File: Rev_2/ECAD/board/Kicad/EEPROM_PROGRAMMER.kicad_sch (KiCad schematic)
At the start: 27 parts, among them Q1 PMOS, Q2 PNP, Q3 PNP, U1 FT232RL, U2 ATMega328P-AU, U3 ICSP, U4 SD_CARD_READER, Y1 16MHz

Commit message: Adde Summer, Read-LED, Write-LED
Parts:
- added D5: READ, LED_SMD:LED_0805_2012Metric_Pad1.15x1.40mm_HandSolder, symbol Device:LED
- added D6: WRITE, LED_SMD:LED_0805_2012Metric_Pad1.15x1.40mm_HandSolder, symbol Device:LED
- added Q4: NPN, Package_TO_SOT_SMD:SOT-23, symbol Simulation_SPICE:NPN
- added R10, R9: 4k7, Resistor_SMD:R_0805_2012Metric_Pad1.20x1.40mm_HandSolder, symbol Device:R
- added R11, R8: 10k, Resistor_SMD:R_0805_2012Metric_Pad1.20x1.40mm_HandSolder, symbol Device:R
- added U5: SUM, EEPROM_PROGRAMMER:Summer, symbol EEPROM_PROGRAMMER:Summer
- R1, R2, R3, R5, R6: value 5k1 -> 4k7
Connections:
- net D11/MOSI: now also R10.2
- net D12/MISO: now also R9.2
- net D13/SCK: now also R8.2
- net GND: now also Q4.3 (E)
- net SELECT: now reaches U2.14 ((SS)PB2), U4.4 (#CS)
- net SELECT: now also R11.2
- new net: D5.2 (A), R9.1
- new net: Q4.2 (B), R11.1
- new net: R8.1, U5.1 (+)
- new net: D6.2 (A), R10.1
- new net SELECT_GND: D5.1 (K), D6.1 (K), Q4.1 (C), U5.2 (-)

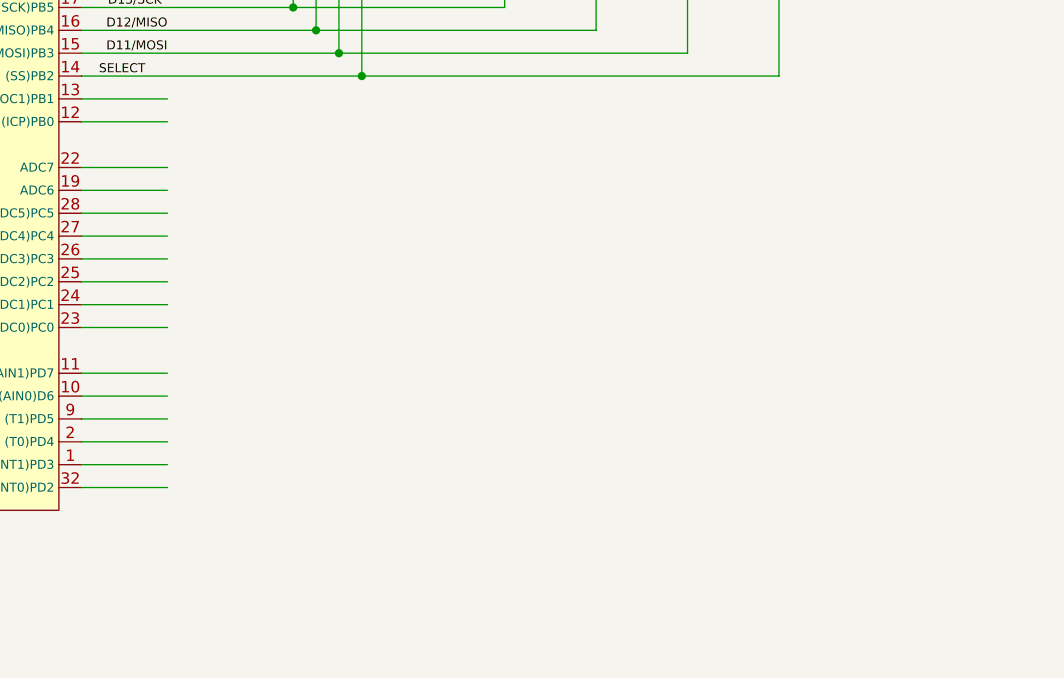
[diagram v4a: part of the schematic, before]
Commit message: Added registers for the EEPROM
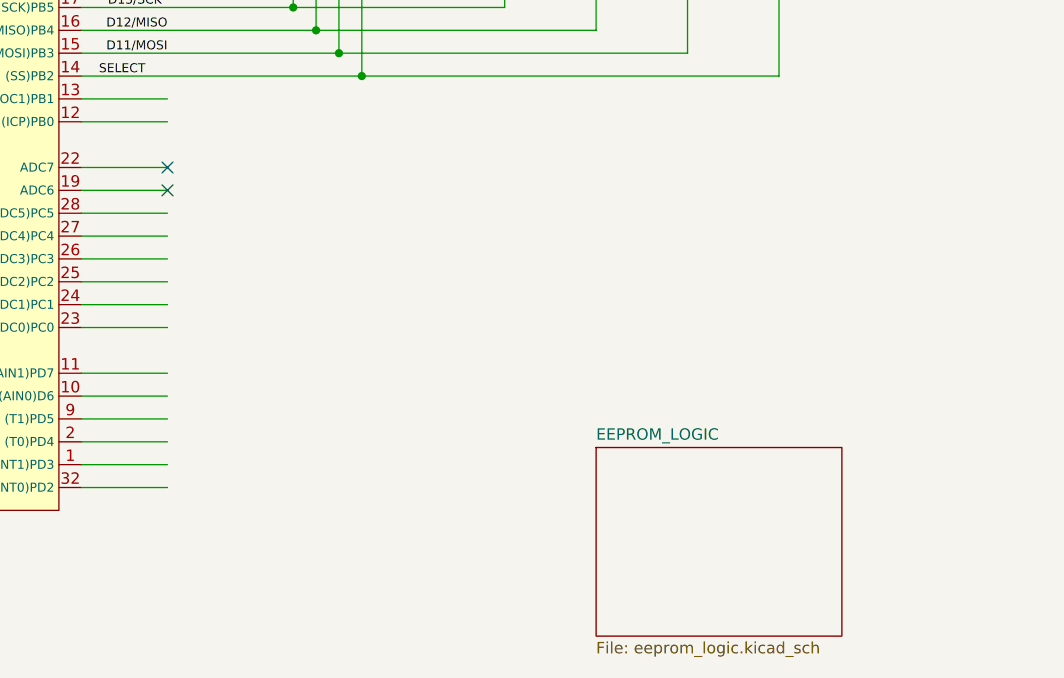
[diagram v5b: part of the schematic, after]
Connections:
- no-connect marks 1 -> 3
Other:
- added sheet EEPROM_LOGIC (eeprom_logic.kicad_sch)
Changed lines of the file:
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@@
   )
   (no_connect (at 31.75 48.895))
+  (no_connect (at 95.25 161.29))
+  (no_connect (at 95.25 158.75))
   (wire (pts (xy 78.74 46.355) (xy 78.74 50.8))
     (stroke (width 0) (type default))
@@
       )
     )
+  )
+  (sheet (at 142.875 189.865) (size 27.305 20.955) (fields_autoplaced)
+    (stroke (width 0.1524) (type solid))
+    (fill (color 0 0 0 0.0000))
+    (property "Sheetname" "EEPROM_LOGIC" (at 142.875 189.1534 0)
+      (effects (font (size 1.27 1.27)) (justify left bottom))
+    )
+    (property "Sheetfile" "eeprom_logic.kicad_sch" (at 142.875 211.4046 0)
+      (effects (font (size 1.27 1.27)) (justify left top))
+    )
+    (instances
+      (project "EEPROM_PROGRAMMER"
+        (path "/bc7d165f-daf1-4bac-b7f4-5fbe134c87cf" (page "2"))
+      )
+    )

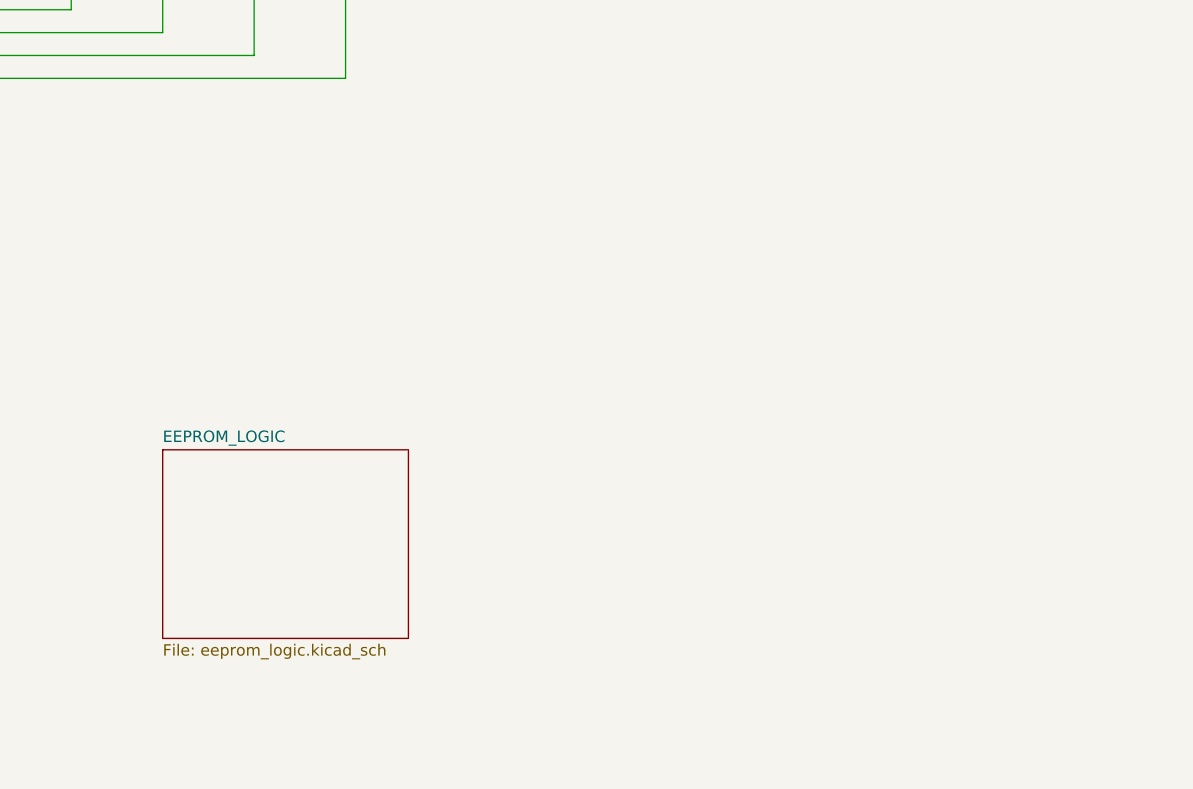
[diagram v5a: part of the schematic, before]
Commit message: Finished most of EEPROM LOGIC
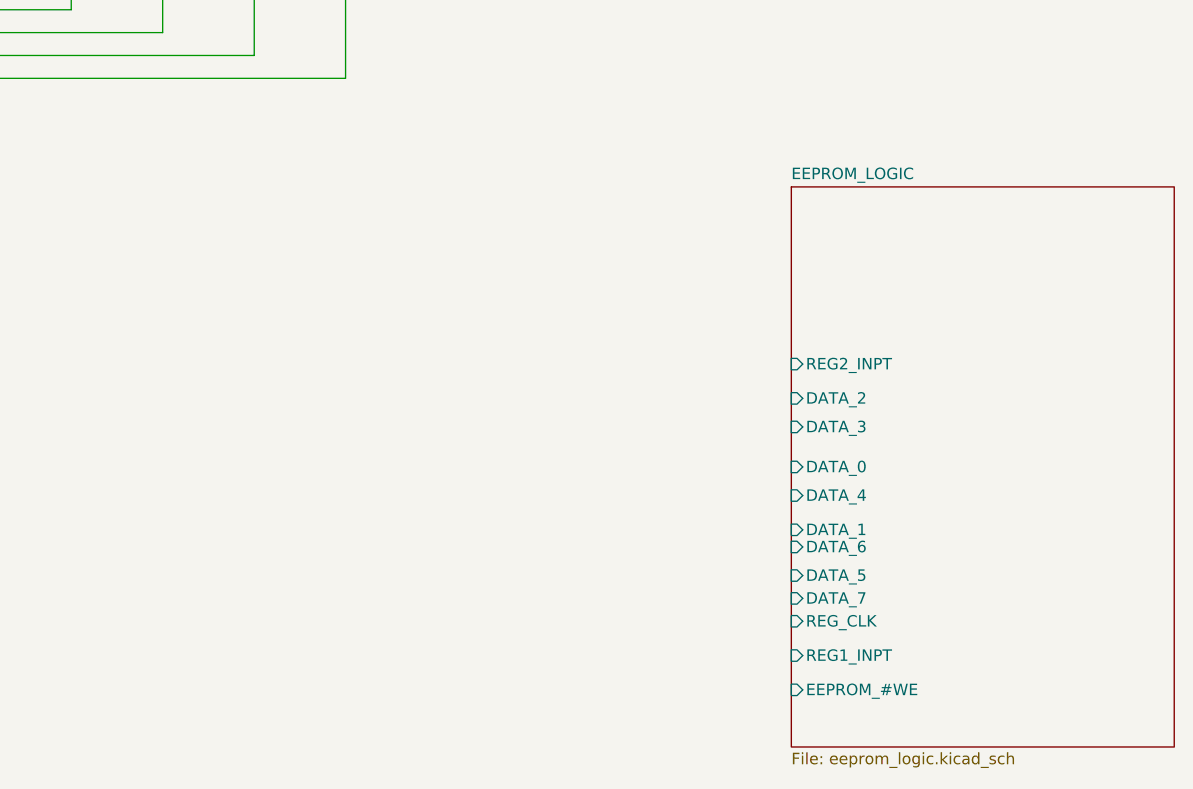
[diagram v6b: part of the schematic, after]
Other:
- sheet EEPROM_LOGIC ports: added DATA_0, DATA_1, DATA_2, DATA_3, DATA_4, DATA_5, DATA_6, DATA_7, EEPROM_#WE, REG1_INPT, REG2_INPT, REG_CLK; removed none
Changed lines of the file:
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@@
     )
   )
-  (sheet (at 142.875 189.865) (size 27.305 20.955) (fields_autoplaced)
+  (sheet (at 212.725 160.655) (size 42.545 62.23) (fields_autoplaced)
     (stroke (width 0.1524) (type solid))
     (fill (color 0 0 0 0.0000))
-    (property "Sheetname" "EEPROM_LOGIC" (at 142.875 189.1534 0)
+    (property "Sheetname" "EEPROM_LOGIC" (at 212.725 159.9434 0)
       (effects (font (size 1.27 1.27)) (justify left bottom))
     )
-    (property "Sheetfile" "eeprom_logic.kicad_sch" (at 142.875 211.4046 0)
+    (property "Sheetfile" "eeprom_logic.kicad_sch" (at 212.725 223.4696 0)
       (effects (font (size 1.27 1.27)) (justify left top))
     )
+    (pin "EEPROM_#WE" input (at 212.725 216.535 180)
+      (effects (font (size 1.27 1.27)) (justify left))
+    )
+    (pin "REG1_INPT" input (at 212.725 212.725 180)
+      (effects (font (size 1.27 1.27)) (justify left))
+    )
+    (pin "REG_CLK" input (at 212.725 208.915 180)
+      (effects (font (size 1.27 1.27)) (justify left))
+    )
+    (pin "DATA_7" input (at 212.725 206.375 180)
+      (effects (font (size 1.27 1.27)) (justify left))
+    )
+    (pin "DATA_5" input (at 212.725 203.835 180)
+      (effects (font (size 1.27 1.27)) (justify left))
+    )
+    (pin "DATA_6" input (at 212.725 200.66 180)
+      (effects (font (size 1.27 1.27)) (justify left))
+    )
+    (pin "DATA_1" input (at 212.725 198.755 180)
+      (effects (font (size 1.27 1.27)) (justify left))
+    )
+    (pin "DATA_4" input (at 212.725 194.945 180)
+      (effects (font (size 1.27 1.27)) (justify left))
+    )
+    (pin "DATA_0" input (at 212.725 191.77 180)
+      (effects (font (size 1.27 1.27)) (justify left))
+    )
+    (pin "DATA_3" input (at 212.725 187.325 180)
+      (effects (font (size 1.27 1.27)) (justify left))
+    )
+    (pin "DATA_2" input (at 212.725 184.15 180)
+      (effects (font (size 1.27 1.27)) (justify left))
+    )
+    (pin "REG2_INPT" input (at 212.725 180.34 180)
+      (effects (font (size 1.27 1.27)) (justify left))
+    )
     (instances

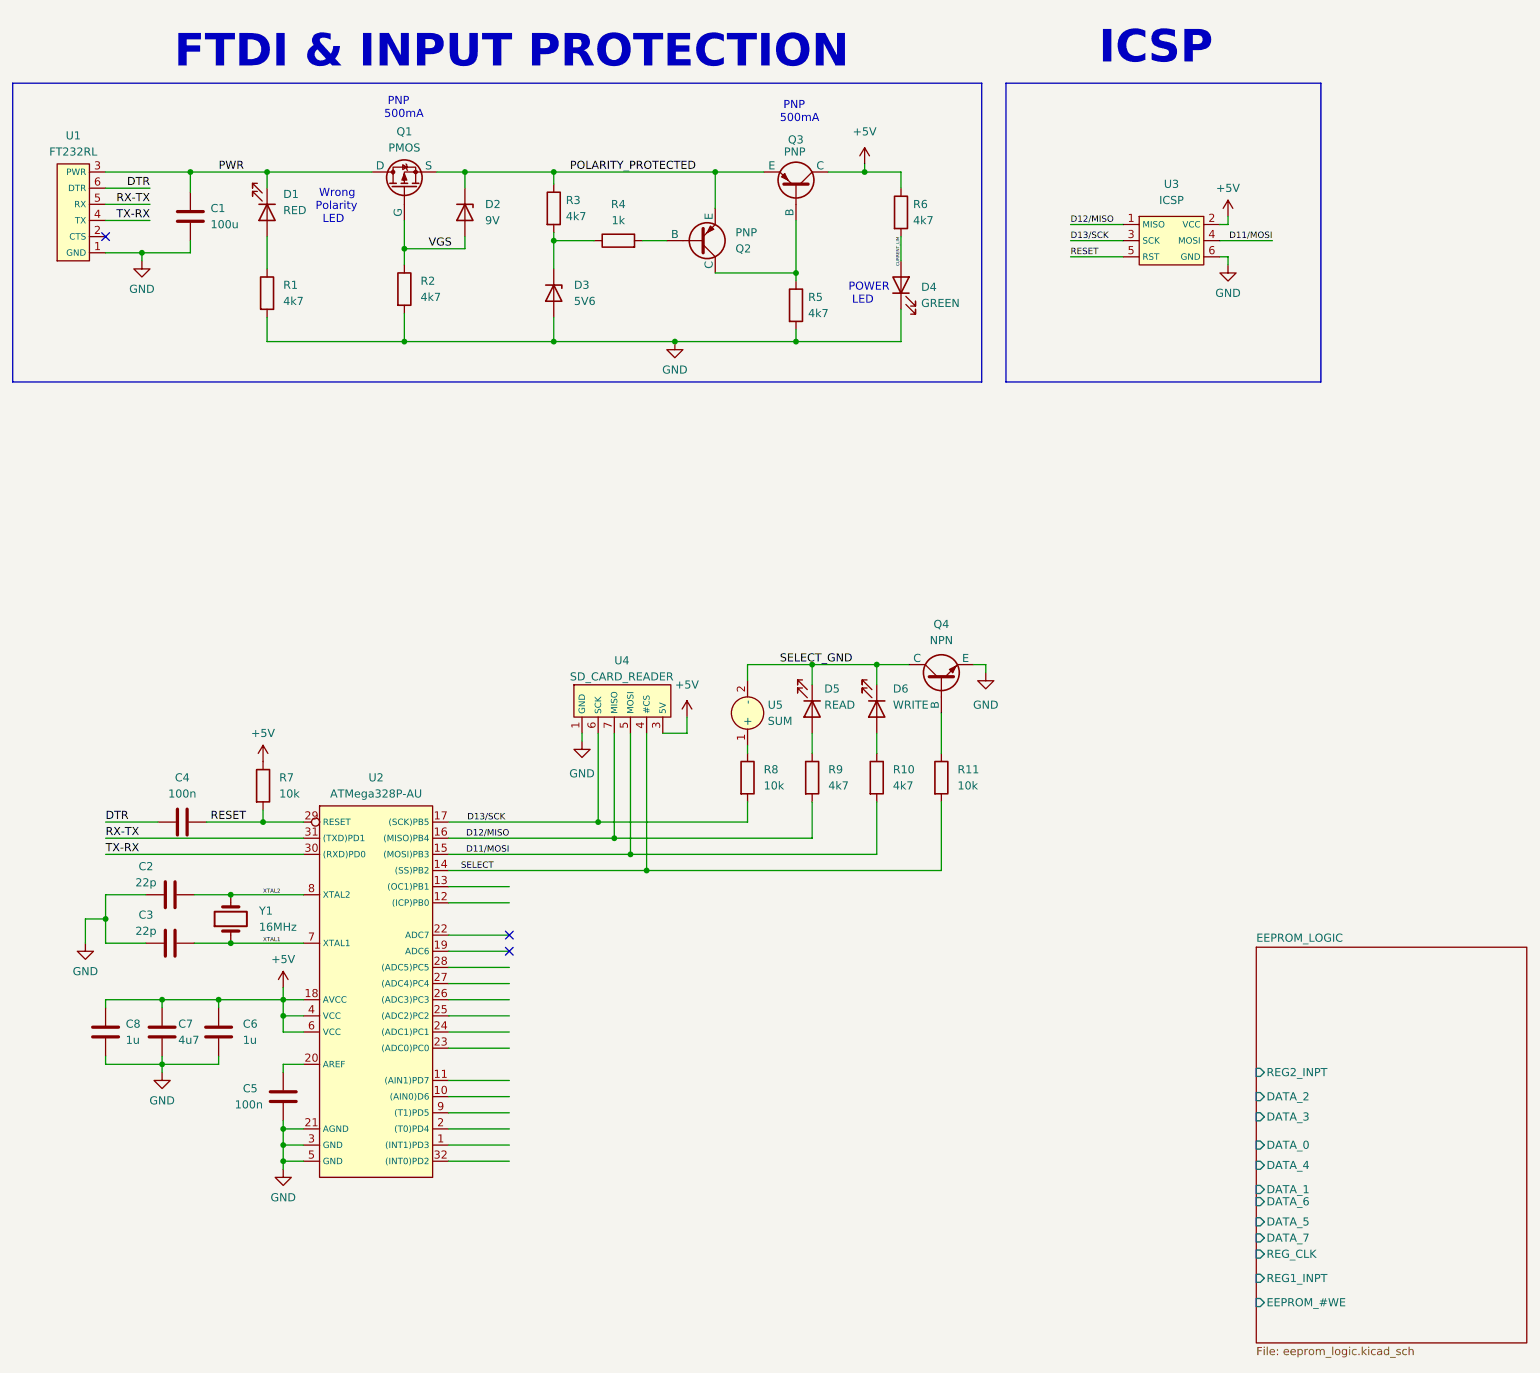
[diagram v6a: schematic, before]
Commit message: Atmega to logic wiring completed
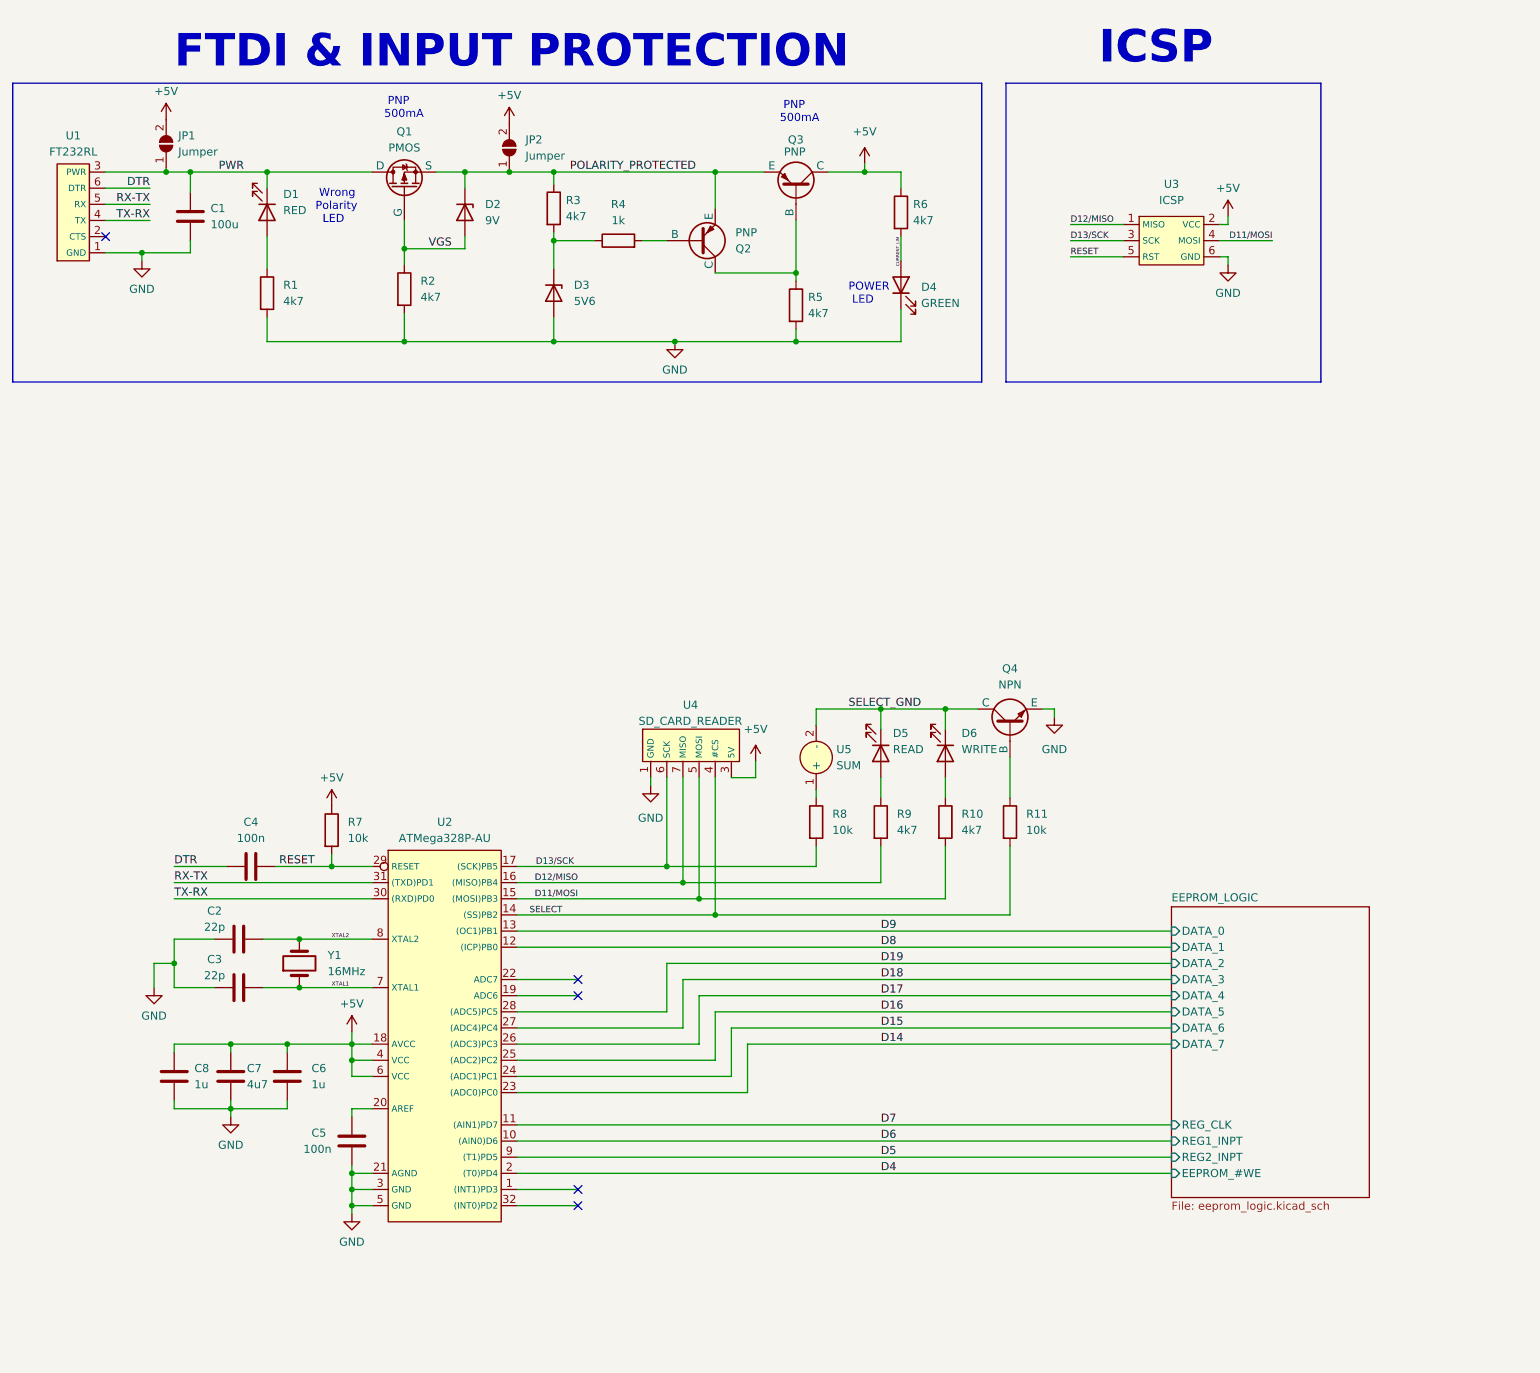
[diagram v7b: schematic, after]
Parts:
- added JP1, JP2: Jumper, Jumper:SolderJumper-2_P1.3mm_Open_TrianglePad1.0x1.5mm, symbol Jumper:SolderJumper_2_Open
- Y1: footprint (none) -> EEPROM_PROGRAMMER:Crystal
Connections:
- net +5V: now also JP1.2 (B), JP2.2 (B)
- net POLARITY_PROTECTED: now also JP2.1 (A)
- net PWR: now also JP1.1 (A)
- net D6: now reaches U2.10 ((AIN0)D6)
- net D7: now reaches U2.11 ((AIN1)PD7)
- net D8: now reaches U2.12 ((ICP)PB0)
- net D9: now reaches U2.13 ((OC1)PB1)
- net D4: now reaches U2.2 ((T0)PD4)
- net D14: now reaches U2.23 ((ADC0)PC0)
- net D15: now reaches U2.24 ((ADC1)PC1)
- net D16: now reaches U2.25 ((ADC2)PC2)
- net D17: now reaches U2.26 ((ADC3)PC3)
- net D18: now reaches U2.27 ((ADC4)PC4)
- net D19: now reaches U2.28 ((ADC5)PC5)
- net D5: now reaches U2.9 ((T1)PD5)
- no-connect marks 3 -> 5
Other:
- moved on the sheet: C2, C3, C4, C5, C6, C7, C8, D5, D6, Q4, R10, R11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
